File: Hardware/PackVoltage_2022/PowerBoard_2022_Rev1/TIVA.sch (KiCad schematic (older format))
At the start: 1 part, among them U54 TM4C129E_Launchpad

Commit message: Actuation shit
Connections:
- net Driver_GimAct: now reaches U54.PA4 (B2_9)
- net Current_Sensor_Gimbal renamed Current_Sensor_GimAct
- net Current_Sensor_SciLog renamed Current_Sensor_SciAct
- net Driver_SciLog renamed Driver_SciAct
- no-connect marks 35 -> 34
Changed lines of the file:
@@
 Driver_SciSensor
 Text HLabel 8100 2500 2    50   Input ~ 0
-Current_Sensor_Gimbal
+Current_Sensor_GimAct
 Text HLabel 6900 2300 0    50   Output ~ 0
 Driver_Gimbal
@@
 Driver_Drive
 Text HLabel 3400 3850 0    50   Input ~ 0
-Current_Sensor_SciLog
+Current_Sensor_SciAct
 Text HLabel 6900 2900 0    50   Output ~ 0
-Driver_SciLog
+Driver_SciAct
 Wire Wire Line
 	5000 2100 4450 2100
@@
 NoConn ~ 4450 2800
 NoConn ~ 4450 2700
-NoConn ~ 4450 4550
 NoConn ~ 4450 4650
 NoConn ~ 8000 2100
@@
 NoConn ~ 8000 4250
 NoConn ~ 8000 4150
+Wire Wire Line
+	4450 4550 4550 4550
+Text HLabel 4550 4550 2    50   Output ~ 0
+Driver_GimAct
 $EndSCHEMATC

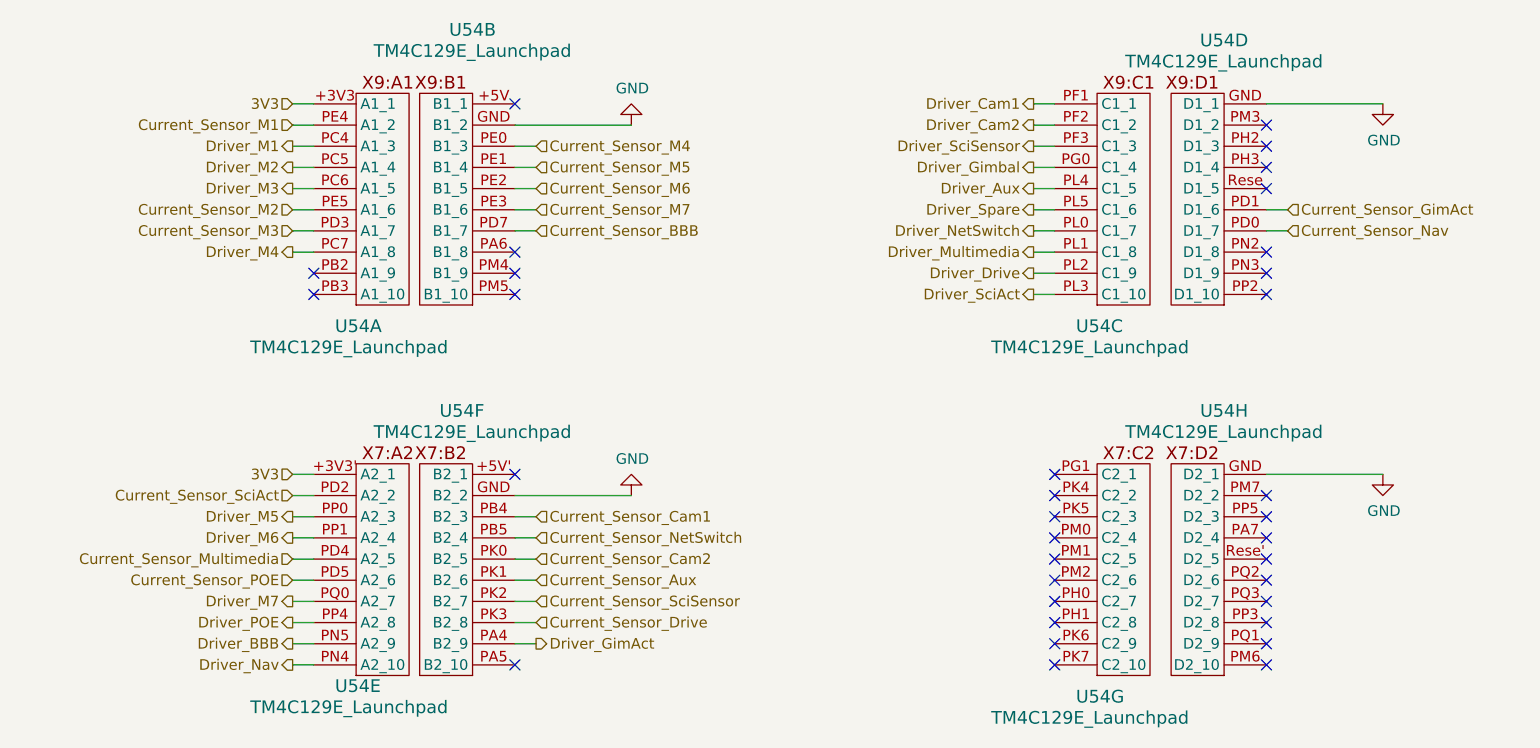
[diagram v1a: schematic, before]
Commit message: Made it to layout, found out about gnd via
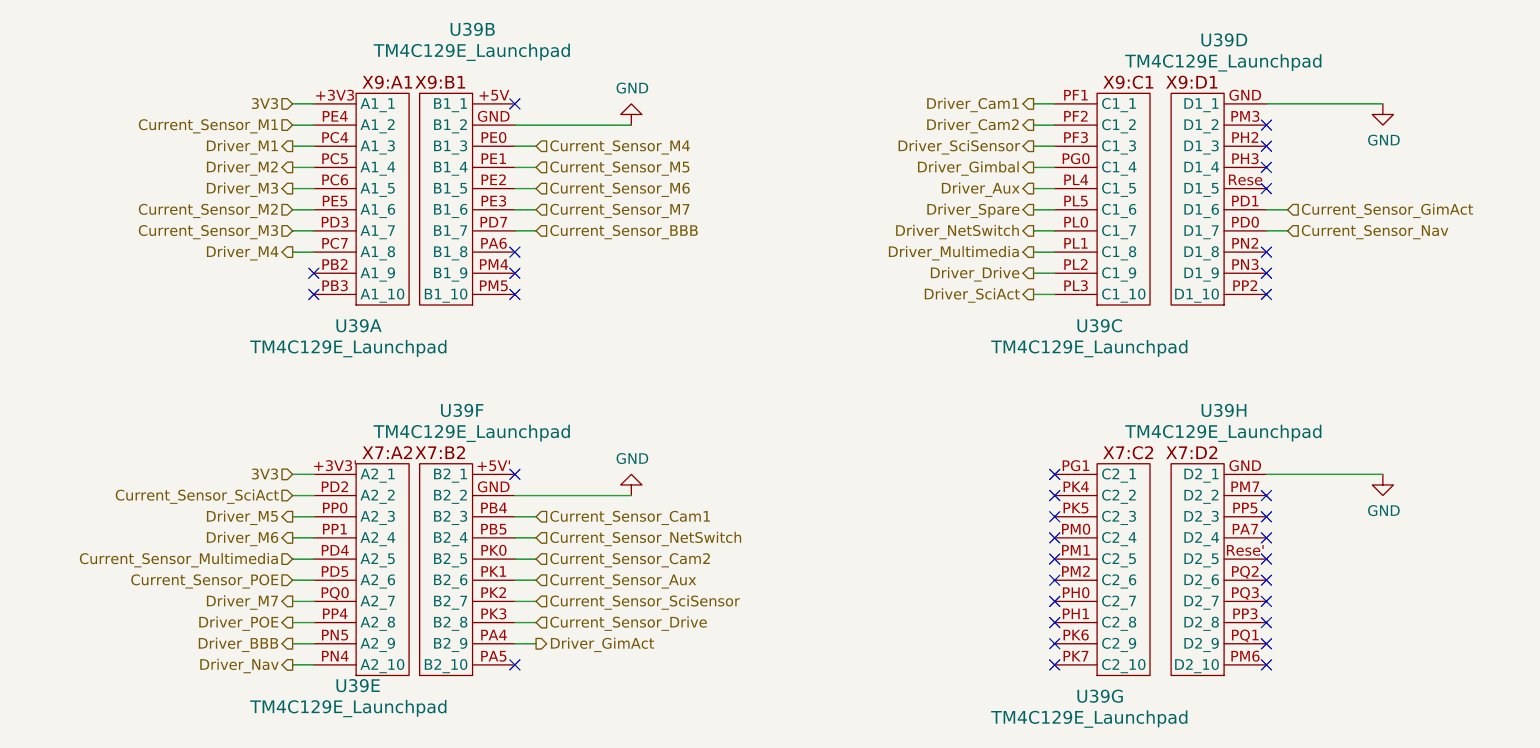
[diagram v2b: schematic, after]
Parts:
- renumbered U54 to U39
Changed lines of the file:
@@
 $EndDescr
 $Comp
-L PowerBoard_2022_Rev1-rescue:TM4C129E_Launchpad-MRDT_Shields U54
+L PowerBoard_2022_Rev1-rescue:TM4C129E_Launchpad-MRDT_Shields U39
 U 1 1 6158A6C0
 P 3700 2950
-F 0 "U54" H 3600 2850 60  0000 L CNN
+F 0 "U39" H 3600 2850 60  0000 L CNN
 F 1 "TM4C129E_Launchpad" H 3200 2750 60  0000 L CNN
 F 2 "MRDT_Shields:TM4C129E_Launchpad_FULL_THT_TOP" H 3700 2950 60  0001 C CNN
@@
 $EndComp
 $Comp
-L PowerBoard_2022_Rev1-rescue:TM4C129E_Launchpad-MRDT_Shields U54
+L PowerBoard_2022_Rev1-rescue:TM4C129E_Launchpad-MRDT_Shields U39
 U 3 1 6158D78C
 P 7200 2950
-F 0 "U54" H 7100 2850 60  0000 L CNN
+F 0 "U39" H 7100 2850 60  0000 L CNN
 F 1 "TM4C129E_Launchpad" H 6700 2750 60  0000 L CNN
 F 2 "MRDT_Shields:TM4C129E_Launchpad_FULL_THT_TOP" H 7200 2950 60  0001 C CNN
@@
 $EndComp
 $Comp
-L PowerBoard_2022_Rev1-rescue:TM4C129E_Launchpad-MRDT_Shields U54
+L PowerBoard_2022_Rev1-rescue:TM4C129E_Launchpad-MRDT_Shields U39
 U 5 1 6159114C
 P 3700 4700
-F 0 "U54" H 3600 4650 60  0000 L CNN
+F 0 "U39" H 3600 4650 60  0000 L CNN
 F 1 "TM4C129E_Launchpad" H 3200 4550 60  0000 L CNN
 F 2 "MRDT_Shields:TM4C129E_Launchpad_FULL_THT_TOP" H 3700 4700 60  0001 C CNN
@@
 $EndComp
 $Comp
-L PowerBoard_2022_Rev1-rescue:TM4C129E_Launchpad-MRDT_Shields U54
+L PowerBoard_2022_Rev1-rescue:TM4C129E_Launchpad-MRDT_Shields U39
 U 7 1 6159532D
 P 7200 4700
-F 0 "U54" H 7100 4600 60  0000 L CNN
+F 0 "U39" H 7100 4600 60  0000 L CNN
 F 1 "TM4C129E_Launchpad" H 6700 4500 60  0000 L CNN
 F 2 "MRDT_Shields:TM4C129E_Launchpad_FULL_THT_TOP" H 7200 4700 60  0001 C CNN
@@
 $EndComp
 $Comp
-L PowerBoard_2022_Rev1-rescue:TM4C129E_Launchpad-MRDT_Shields U54
+L PowerBoard_2022_Rev1-rescue:TM4C129E_Launchpad-MRDT_Shields U39
 U 4 1 6159FCAE
 P 7800 2950
-F 0 "U54" H 7800 4200 60  0000 C CNN
+F 0 "U39" H 7800 4200 60  0000 C CNN
 F 1 "TM4C129E_Launchpad" H 7800 4100 60  0000 C CNN
 F 2 "MRDT_Shields:TM4C129E_Launchpad_FULL_THT_TOP" H 7800 2950 60  0001 C CNN
@@
 $EndComp
 $Comp
-L PowerBoard_2022_Rev1-rescue:TM4C129E_Launchpad-MRDT_Shields U54
+L PowerBoard_2022_Rev1-rescue:TM4C129E_Launchpad-MRDT_Shields U39
 U 6 1 615A50D2
 P 4250 4700
-F 0 "U54" H 4300 5950 60  0000 C CNN
+F 0 "U39" H 4300 5950 60  0000 C CNN
 F 1 "TM4C129E_Launchpad" H 4250 5850 60  0000 C CNN
 F 2 "MRDT_Shields:TM4C129E_Launchpad_FULL_THT_TOP" H 4250 4700 60  0001 C CNN
@@
 $EndComp
 $Comp
-L PowerBoard_2022_Rev1-rescue:TM4C129E_Launchpad-MRDT_Shields U54
+L PowerBoard_2022_Rev1-rescue:TM4C129E_Launchpad-MRDT_Shields U39
 U 8 1 615A8D41
 P 7800 4700
-F 0 "U54" H 7800 5950 60  0000 C CNN
+F 0 "U39" H 7800 5950 60  0000 C CNN
 F 1 "TM4C129E_Launchpad" H 7800 5850 60  0000 C CNN
 F 2 "MRDT_Shields:TM4C129E_Launchpad_FULL_THT_TOP" H 7800 4700 60  0001 C CNN
@@
 $EndComp
 $Comp
-L PowerBoard_2022_Rev1-rescue:TM4C129E_Launchpad-MRDT_Shields U54
+L PowerBoard_2022_Rev1-rescue:TM4C129E_Launchpad-MRDT_Shields U39
 U 2 1 6159A0CA
 P 4250 2950
-F 0 "U54" H 4250 4250 60  0000 C CNN
+F 0 "U39" H 4250 4250 60  0000 C CNN
 F 1 "TM4C129E_Launchpad" H 4250 4150 60  0000 C CNN
 F 2 "MRDT_Shields:TM4C129E_Launchpad_FULL_THT_TOP" H 4250 2950 60  0001 C CNN
@@
 	3400 3750 3500 3750
 $Comp
-L power:GND #PWR0233
+L power:GND #PWR0103
 U 1 1 61617E3D
 P 5000 3850
-F 0 "#PWR0233" H 5000 3600 50  0001 C CNN
+F 0 "#PWR0103" H 5000 3600 50  0001 C CNN
 F 1 "GND" H 5005 3677 50  0000 C CNN
 F 2 "" H 5000 3850 50  0001 C CNN
@@
 	5000 3850 4450 3850
 $Comp
-L power:GND #PWR0234
+L power:GND #PWR0104
 U 1 1 61619BA9
 P 8550 2000
-F 0 "#PWR0234" H 8550 1750 50  0001 C CNN
+F 0 "#PWR0104" H 8550 1750 50  0001 C CNN
 F 1 "GND" H 8555 1827 50  0000 C CNN
 F 2 "" H 8550 2000 50  0001 C CNN
@@
 	8550 2000 8000 2000
 $Comp
-L power:GND #PWR0235
+L power:GND #PWR0105
 U 1 1 6161A1E2
 P 8550 3750
-F 0 "#PWR0235" H 8550 3500 50  0001 C CNN
+F 0 "#PWR0105" H 8550 3500 50  0001 C CNN
 F 1 "GND" H 8555 3577 50  0000 C CNN
 F 2 "" H 8550 3750 50  0001 C CNN
@@
 	5000 2100 4450 2100
 $Comp
-L power:GND #PWR0236
+L power:GND #PWR0102
 U 1 1 61619870
 P 5000 2100
-F 0 "#PWR0236" H 5000 1850 50  0001 C CNN
+F 0 "#PWR0102" H 5000 1850 50  0001 C CNN
 F 1 "GND" H 5005 1927 50  0000 C CNN
 F 2 "" H 5000 2100 50  0001 C CNN

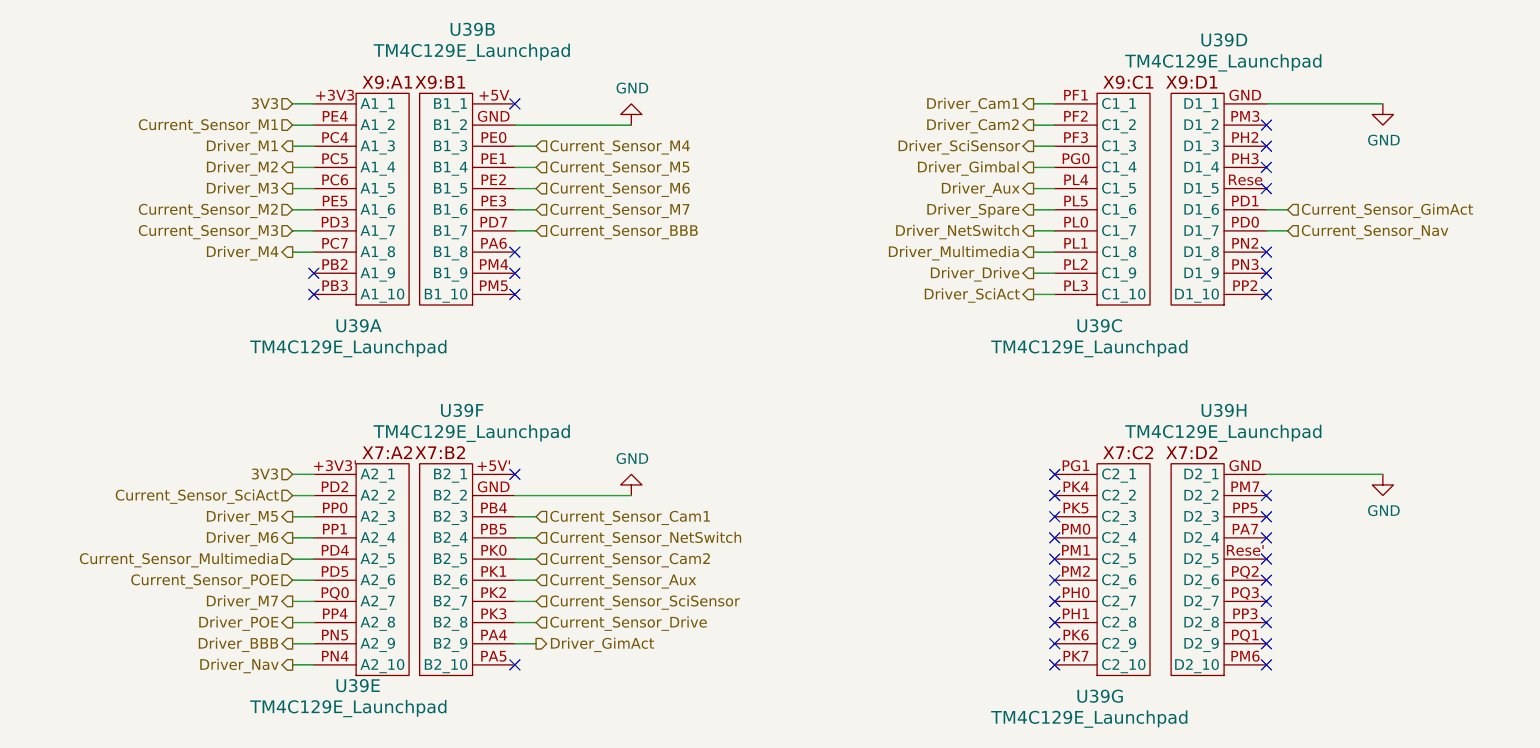
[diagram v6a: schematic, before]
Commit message: Connected the TIVA up
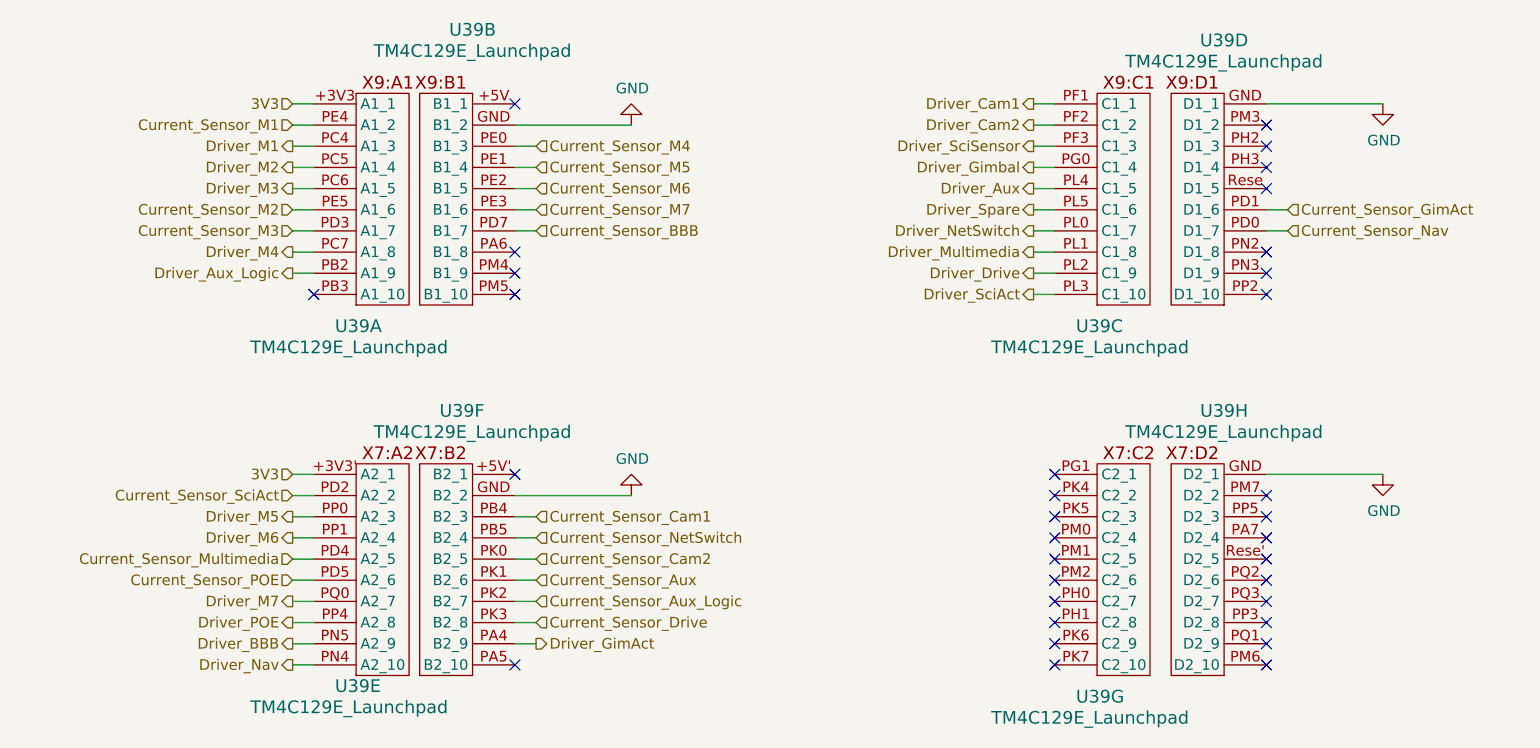
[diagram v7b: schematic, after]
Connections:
- net Driver_Aux_Logic: now reaches U39.PB2 (A1_9)
- net Current_Sensor_SciSensor renamed Current_Sensor_Aux_Logic
- no-connect marks 34 -> 33
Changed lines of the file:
@@
 Driver_Cam2
 Text HLabel 4550 4350 2    50   Input ~ 0
-Current_Sensor_SciSensor
+Current_Sensor_Aux_Logic
 Text HLabel 6900 2200 0    50   Output ~ 0
 Driver_SciSensor
@@
 Wire Wire Line
 	4550 2600 4450 2600
-NoConn ~ 3500 2800
 NoConn ~ 3500 2900
 NoConn ~ 4450 2900
@@
 Text HLabel 4550 4550 2    50   Output ~ 0
 Driver_GimAct
+Text HLabel 3400 2800 0    50   Output ~ 0
+Driver_Aux_Logic
+Wire Wire Line
+	3400 2800 3500 2800
 $EndSCHEMATC
